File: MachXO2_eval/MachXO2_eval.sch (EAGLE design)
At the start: 34 parts, among them CN1 I2C_IF, CN2 POWER_IF, CN3 LCMXO2-CN2, CN4 LCMXO2-CN1, U1 LCMXO2-256HC-4TG100C, U2 AE-FT2232, U3 XC6202P332TH

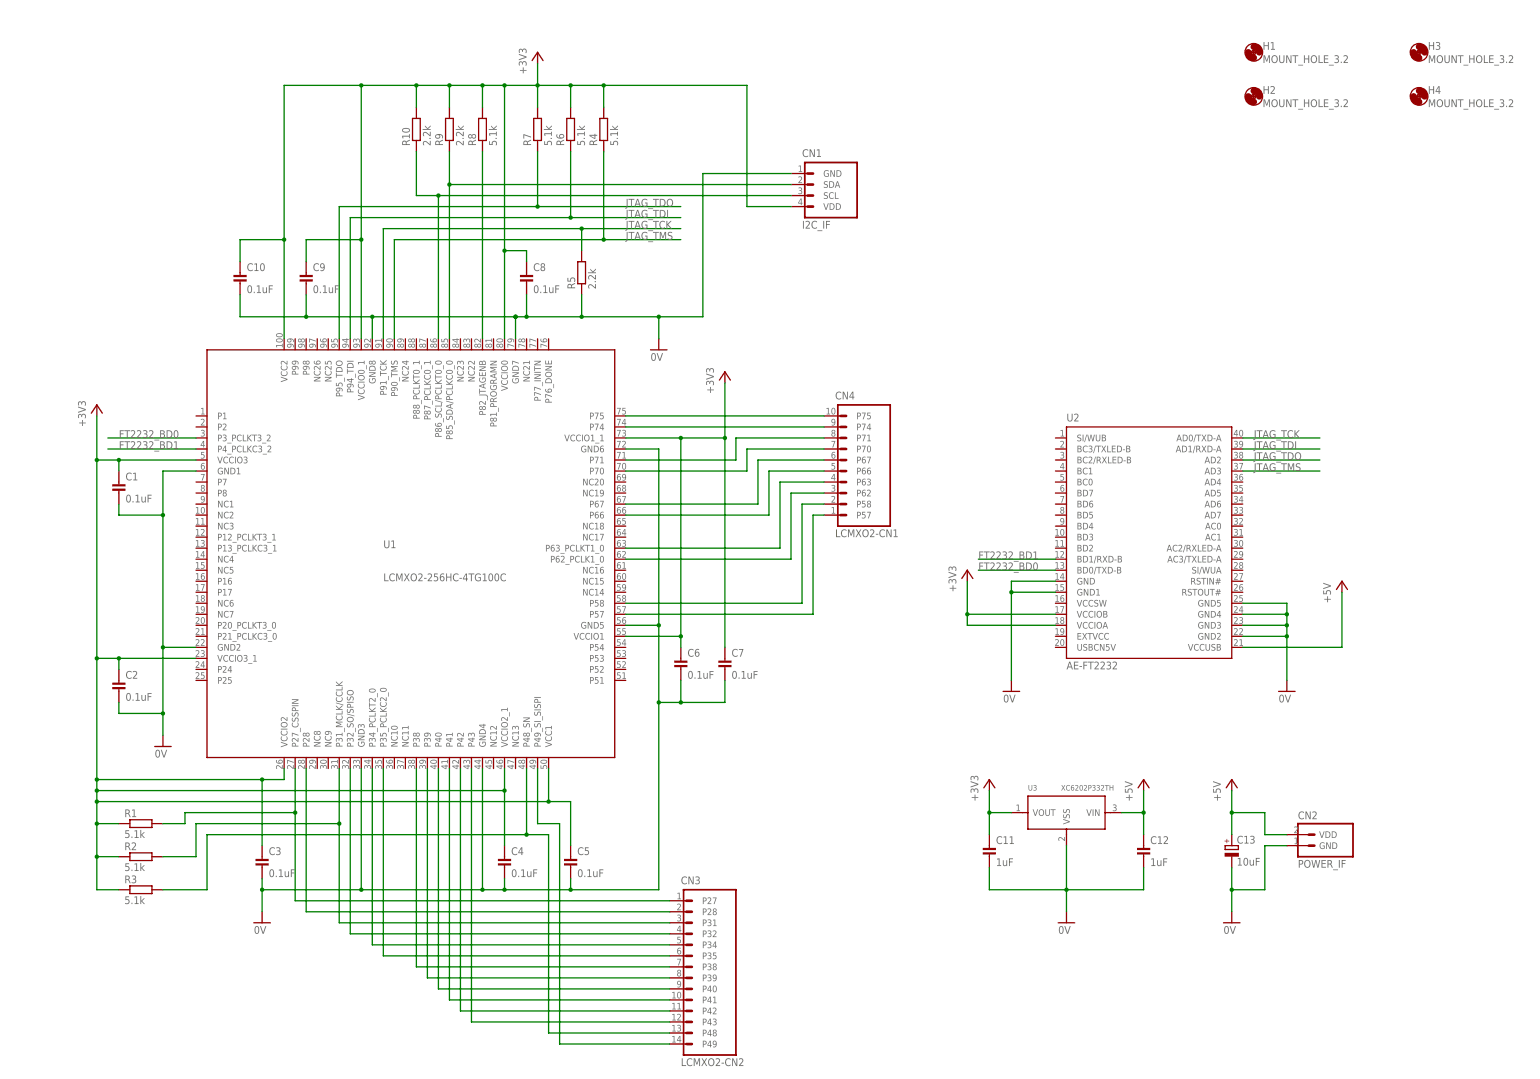
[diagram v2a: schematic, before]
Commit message: MachXO2評価基板修正
外出し用のピンを追加
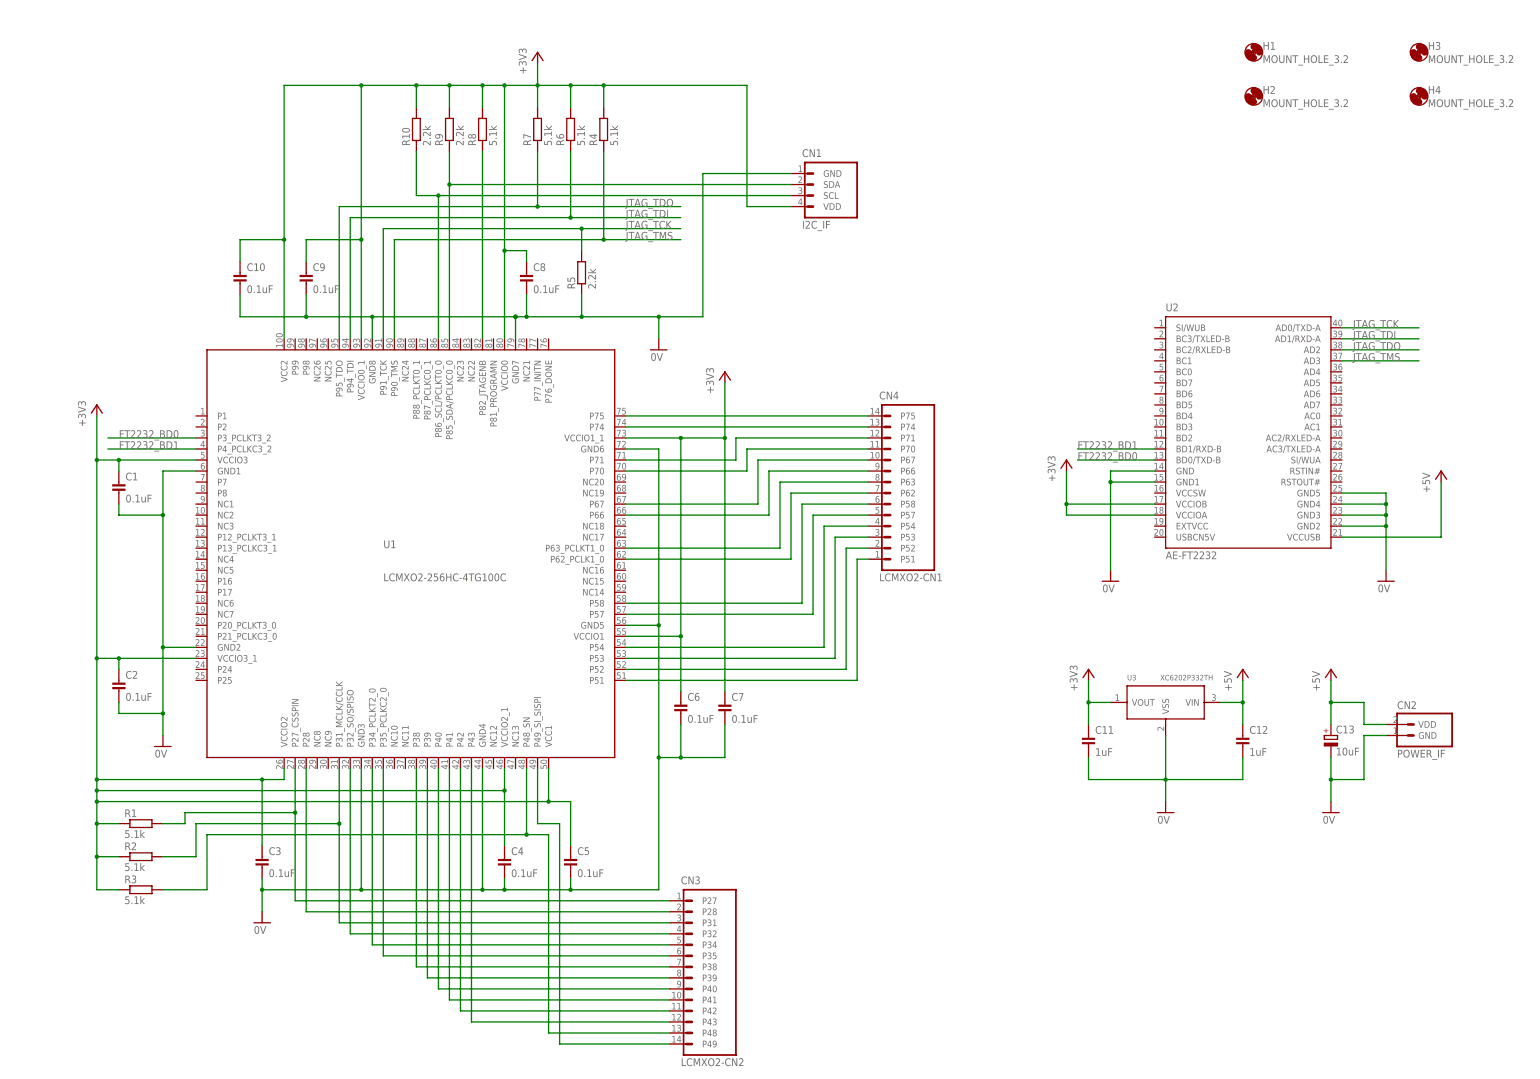
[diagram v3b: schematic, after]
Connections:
- new net N$15: CN4.P52, U1.P52
- new net N$16: CN4.P51, U1.P51
- new net N$4: CN4.P54, U1.P54
- new net N$5: CN4.P53, U1.P53
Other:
- moved on the sheet: C11, C12, C13, C6, C7, CN2, U2, U3

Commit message: MachXO2評価基板修正
外出し用のピンをさらに追加
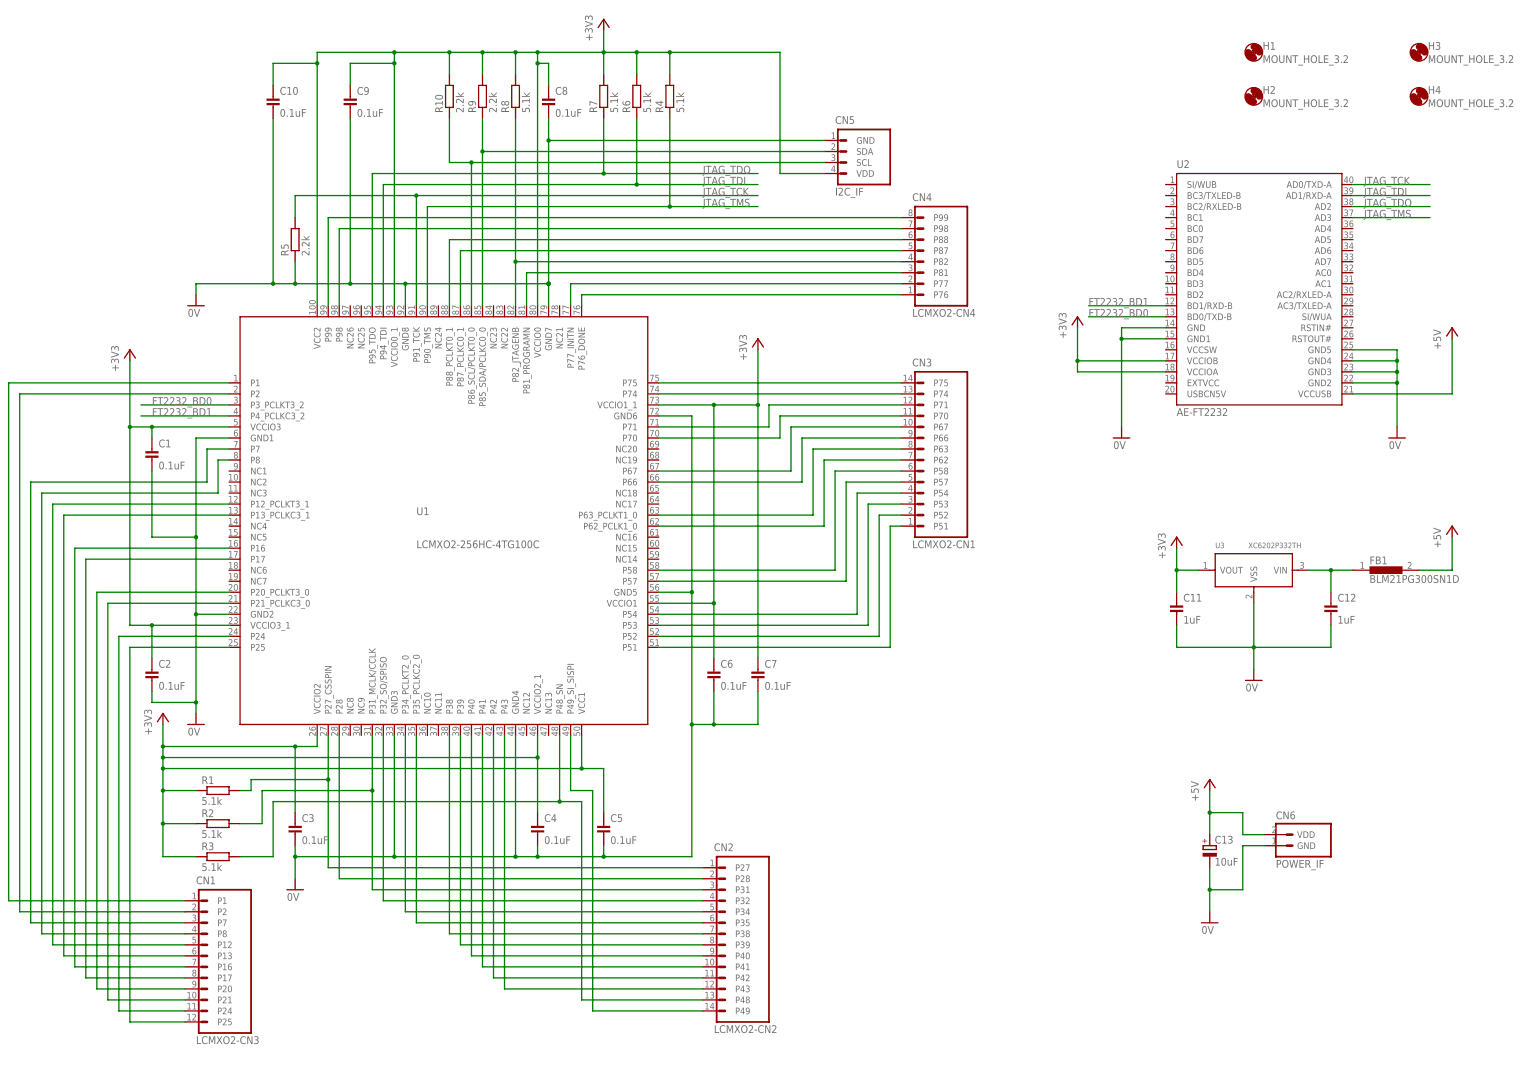
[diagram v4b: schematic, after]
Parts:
- added CN5: I2C_IF, PartsForProto:I2C_IF
- added CN6: POWER_IF, PartsForProto:POWER_IF
- added FB1: BLM21PG300SN1D, Parts:BLM21PG300SN1D
- CN1: value I2C_IF -> LCMXO2-CN3; device PartsForProto:I2C_IF -> PartsForProto:LCMXO2-CN3
- CN2: value POWER_IF -> LCMXO2-CN2; device PartsForProto:POWER_IF -> PartsForProto:LCMXO2-CN2
- CN3: value LCMXO2-CN2 -> LCMXO2-CN1; device PartsForProto:LCMXO2-CN2 -> PartsForProto:LCMXO2-CN1
- CN4: value LCMXO2-CN1 -> LCMXO2-CN4; device PartsForProto:LCMXO2-CN1 -> PartsForProto:LCMXO2-CN4
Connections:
- new net N$31: CN4.P76, U1.P76_DONE
- new net N$32: CN4.P77, U1.P77_INITN
- new net N$33: C12.1, FB1.1, U3.VIN
- new net N$35: CN4.P99, U1.P99
- new net N$36: CN4.P98, U1.P98
- new net N$37: CN4.P88, U1.P88_PCLKT0_1
- new net N$38: CN4.P87, U1.P87_PCLKC0_1
- new net N$39: CN4.P81, U1.P81_PROGRAMN
- new net N$43: CN1.P25, U1.P25
- new net N$44: CN1.P24, U1.P24
- new net N$46: CN1.P21, U1.P21_PCLKC3_0
- new net N$47: CN1.P20, U1.P20_PCLKT3_0
- new net N$48: CN1.P17, U1.P17
- new net N$49: CN1.P16, U1.P16
- new net N$50: CN1.P13, U1.P13_PCLKC3_1
- new net N$51: CN1.P12, U1.P12_PCLKT3_1
- new net N$52: CN1.P8, U1.P8
- new net N$53: CN1.P7, U1.P7
- new net N$54: CN1.P2, U1.P2
- new net N$55: CN1.P1, U1.P1
- net +3V3: now also CN5.VDD; no longer CN1.VDD
- net +5V: now also CN6.VDD, FB1.2; no longer C12.1, CN2.VDD, U3.VIN
- net 0V: now also CN5.GND, CN6.GND; no longer CN1.GND, CN2.GND
- net I2C_SCL: now also CN5.SCL; no longer CN1.SCL
- net N$1: now also CN4.P82
- net N$10: now also CN2.P48; no longer CN3.P48
- net N$11: now also CN3.P57; no longer CN4.P57
- net N$12: now also CN3.P58; no longer CN4.P58
- net N$13: now also CN3.P62; no longer CN4.P62
- net N$14: now also CN2.P49; no longer CN3.P49
- net N$15: now also CN3.P52; no longer CN4.P52
- net N$16: now also CN3.P51; no longer CN4.P51
- net N$17: now also CN2.P43; no longer CN3.P43
- net N$18: now also CN2.P42; no longer CN3.P42
- net N$19: now also CN2.P41; no longer CN3.P41
- net N$2: now also CN5.SDA; no longer CN1.SDA
- net N$20: now also CN2.P40; no longer CN3.P40
- net N$21: now also CN2.P39; no longer CN3.P39
- net N$22: now also CN2.P38; no longer CN3.P38
- net N$23: now also CN3.P74; no longer CN4.P74
- net N$24: now also CN2.P35; no longer CN3.P35
- net N$25: now also CN2.P34; no longer CN3.P34
- net N$26: now also CN2.P32; no longer CN3.P32
- net N$27: now also CN2.P28; no longer CN3.P28
- net N$28: now also CN3.P70; no longer CN4.P70
- net N$29: now also CN3.P71; no longer CN4.P71
- net N$3: now also CN2.P27; no longer CN3.P27
- net N$30: now also CN3.P75; no longer CN4.P75
- net N$4: now also CN3.P54; no longer CN4.P54
- net N$5: now also CN3.P53; no longer CN4.P53
- net N$6: now also CN3.P67; no longer CN4.P67
- net N$7: now also CN3.P66; no longer CN4.P66
- net N$8: now also CN2.P31; no longer CN3.P31
- net N$9: now also CN3.P63; no longer CN4.P63
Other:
- moved on the sheet: C1, C10, C11, C12, C13, C2, C3, C4, C5, C6, C7, C8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
